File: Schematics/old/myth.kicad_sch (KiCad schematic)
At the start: 140 parts, among them J1 Conn_01x08_Male, J10 Conn_02x01, J2 Conn_01x08_Male, J3 Conn_01x08_Male, J4 Conn_01x08_Male, J5 Conn_01x08_Male, J6 Conn_01x08_Male, J7 Conn_01x08_Male, J8 Conn_01x04_Male, J9 Conn_01x04_Male, U1 74AHC02, U10 74HC595, U11 74HC165, U12 74AHC08, U13 74HC238, U14 74HC238, U15 74HC238, U16 4002, U17 74AHC273, U18 74LS32, U19 CD4532BE, U2 74AHC04, U20 74AHC138, U21 74AHC04, U22 74AHC138, U23 74HC238, U24 74HC238, U25 74LS32, U26 4078, U27 74AHC244, U28 74LS08, U29 74AHC138, U3 74HC74, U30 74AHC138, U31 4075, U32 74AHC04, U33 74HC00, U34 74HC163, U35 74AHC138, U36 74AHC138, U37 74HC238, U38 74AHC138, U39 74HC238, U4 74HC32, U40 74AHC02, U41 74AHC574, U42 74HC283, U43 74HC283, U44 74AHC574, U45 74HC193, U46 74HC193, U47 74HC157, U48 74HC157, U49 74HC32, U5 74AHC273, U50 74AHC244, U51 74HC157, U52 74HC157, U53 74HC157, U54 74HC157, U55 74HC02, U56 74HC74, U57 74HC193, U58 74HC193, U59 74HC04, U6 74LS08, U60 4078, U61 4078, U62 74AHC574, U63 74HC193, U64 74HC193, U65 74AHC273, U66 74AHC273, U67 74LS573, U68 74LS21, U69 74AHC244, U7 74AHC08, U70 74AHC04, U71 74AHC04, U72 74LS32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

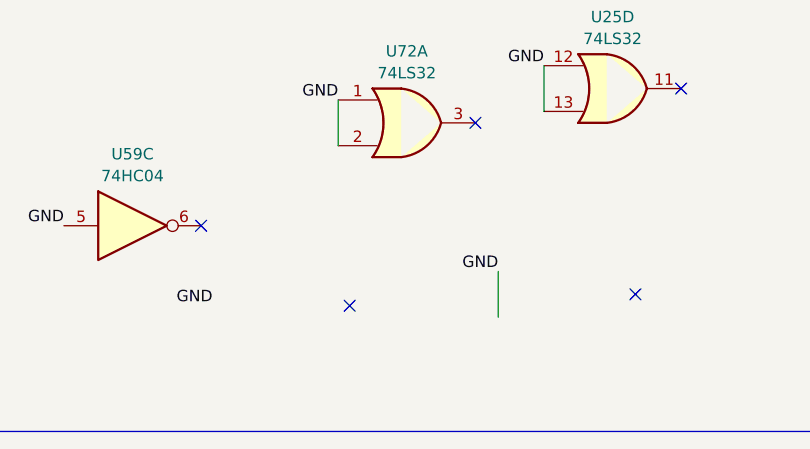
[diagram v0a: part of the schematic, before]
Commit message: Change d to g
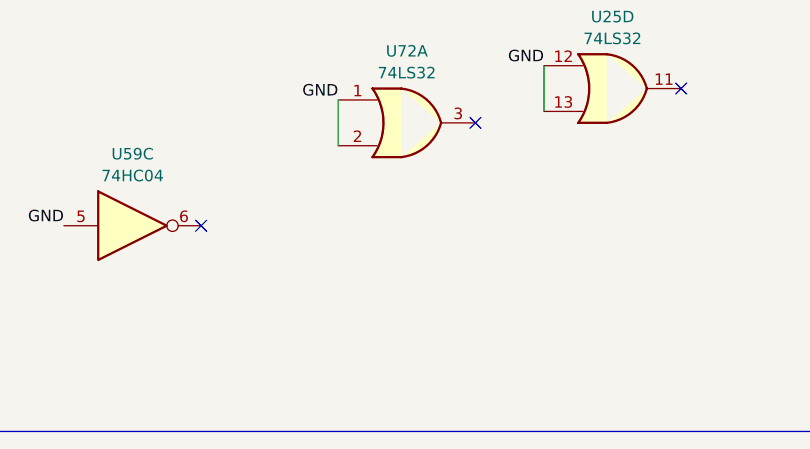
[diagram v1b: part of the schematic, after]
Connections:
- no-connect marks 69 -> 67
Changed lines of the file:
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@@
 	)
 	(no_connect
-		(at 965.2 806.45)
-	)
-	(no_connect
 		(at 137.16 384.81)
 	)
 	(no_connect
-		(at 996.95 805.18)
-	)
-	(no_connect
 		(at 128.27 95.25)
 	)
@@
 	(wire
 		(pts
-			(xy 981.71 802.64) (xy 981.71 807.72)
-		)
-		(stroke
-			(width 0)
-			(type default)
-		)
-	)
-	(wire
-		(pts
 			(xy 227.33 514.35) (xy 227.33 519.43)
 		)
@@
 		)
 	)
-	(label "GND"
-		(at 981.71 802.64 180)
-		(fields_autoplaced yes)
-		(effects
-			(font
-				(size 1.27 1.27)
-			)
-			(justify right bottom)
-		)
-	)
 	(label "+5V"
 		(at 71.12 107.95 180)
@@
 		(fields_autoplaced yes)
 		(effects
-			(font
-				(size 1.27 1.27)
-			)
-			(justify right bottom)
-		)
-	)
-	(label "GND"
-		(at 949.96 806.45 180)
-		(fields_autoplaced yes)
-		(effects

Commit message: Fix bugs in vtable.c
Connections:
- net GETD renamed GETG
- net xD renamed xG
- net ~{BOD} renamed ~{BOG}
- net ~{COD} renamed ~{COG}
- net ~{Dx} renamed ~{Gx}
- net ~{GETD} renamed ~{GETG}
- net ~{PUTD} renamed ~{PUTG}
- net ~{opc_DIRO} renamed ~{opc_GIRO}
- net ~{xD} renamed ~{xG}
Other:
- note added: "(Global) Page Index"
- note added: "G"
- note added: "G/I/R/O"
- note added: "Instruction byte: all0: OPC_SYS 00000 xxx See table @ SYS decoder else: OPC_FIX 00001 x xx b0-1 LSB, b2: Extended sign bit OPC_ALU 0001 xxxx See table @ ALU OPC_TRAP 001 xxxxx b0-4: DEST PAGE OPC_GIRO 01 xx x xxx b0-2 OFFS, b3:GET/PUT, B4-5:REG(GIRO) OPC_PAIR 1 xxx xxxx b0-3 DST, b4-6 SRC"
- note removed: "(DATA) Page Index"
- note removed: "D"
- note removed: "D/I/R/O"
- note removed: "Instruction byte: all0: OPC_SYS 00000 xxx See table @ SYS decoder else: OPC_FIX 00001 x xx b0-1 LSB, b2: Extended sign bit OPC_ALU 0001 xxxx See table @ ALU OPC_TRAP 001 xxxxx b0-4: DEST PAGE OPC_DIRO 01 xx x xxx b0-2 OFFS, b3:GET/PUT, B4-5:REG(DIRO) OPC_PAIR 1 xxx xxxx b0-3 DST, b4-6 SRC"
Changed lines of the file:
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@@
 		)
 	)
-	(text "(DATA)\nPage Index"
+	(text "(Global)\nPage Index"
 		(exclude_from_sim no)
 		(at 886.46 523.24 0)
@@
 		)
 	)
-	(text "D"
+	(text "G"
 		(exclude_from_sim no)
 		(at 871.22 525.78 0)
@@
 		)
 	)
-	(text "                Instruction byte:\nall0: OPC_SYS       00000   xxx    See table @ SYS decoder\nelse: OPC_FIX       00001  x xx    b0-1 LSB, b2: Extended sign bit\n      OPC_ALU       0001   xxxx    See table @ ALU\n      OPC_TRAP      001   xxxxx    b0-4: DEST PAGE\n      OPC_DIRO      01 xx x xxx    b0-2 OFFS, b3:GET/PUT, B4-5:REG(DIRO)\n      OPC_PAIR      1  xxx xxxx    b0-3 DST, b4-6 SRC"
+	(text "                Instruction byte:\nall0: OPC_SYS       00000   xxx    See table @ SYS decoder\nelse: OPC_FIX       00001  x xx    b0-1 LSB, b2: Extended sign bit\n      OPC_ALU       0001   xxxx    See table @ ALU\n      OPC_TRAP      001   xxxxx    b0-4: DEST PAGE\n      OPC_GIRO      01 xx x xxx    b0-2 OFFS, b3:GET/PUT, B4-5:REG(GIRO)\n      OPC_PAIR      1  xxx xxxx    b0-3 DST, b4-6 SRC"
 		(exclude_from_sim no)
 		(at 146.05 571.5 0)
@@
 		)
 	)
-	(text "D/I/R/O"
+	(text "G/I/R/O"
 		(exclude_from_sim no)
 		(at 321.31 471.17 0)
@@
 		)
 	)
-	(label "~{GETD}"
+	(label "~{GETG}"
 		(at 746.76 204.47 180)
 		(fields_autoplaced yes)
@@
 		)
 	)
-	(label "~{COD}"
+	(label "~{COG}"
 		(at 808.99 506.73 180)
 		(fields_autoplaced yes)
@@
 		)
 	)
-	(label "~{GETD}"
+	(label "~{GETG}"
 		(at 353.06 469.9 0)
 		(fields_autoplaced yes)
@@
 		)
 	)
-	(label "~{opc_DIRO}"
+	(label "~{opc_GIRO}"
 		(at 254 504.19 0)
 		(fields_autoplaced yes)
@@
 		)
 	)
-	(label "~{BOD}"
+	(label "~{BOG}"
 		(at 834.39 453.39 0)
 		(fields_autoplaced yes)
@@
 		)
 	)
-	(label "GETD"
+	(label "GETG"
 		(at 762 204.47 0)
 		(fields_autoplaced yes)
@@
 		)
 	)
-	(label "~{Dx}"
+	(label "~{Gx}"
 		(at 361.95 381 0)
 		(fields_autoplaced yes)
@@
 		)
 	)
-	(label "~{opc_DIRO}"
+	(label "~{opc_GIRO}"
 		(at 304.8 480.06 180)
 		(fields_autoplaced yes)
@@
 		)
 	)
-	(label "~{Dx}"
+	(label "~{Gx}"
 		(at 871.22 478.79 0)
 		(fields_autoplaced yes)
@@
 		)
 	)
-	(label "~{PUTD}"
+	(label "~{PUTG}"
 		(at 886.46 481.33 0)
 		(fields_autoplaced yes)
@@
 		)
 	)
-	(label "~{COD}"
+	(label "~{COG}"
 		(at 834.39 448.31 0)
 		(fields_autoplaced yes)
@@
 		)
 	)
-	(label "~{xD}"
+	(label "~{xG}"
 		(at 706.12 218.44 180)
 		(fields_autoplaced yes)
@@
 		)
 	)
-	(label "xD"
+	(label "xG"
 		(at 721.36 218.44 0)
 		(fields_autoplaced yes)
@@
 		)
 	)
-	(label "xD"
+	(label "xG"
 		(at 787.4 499.11 180)
 		(fields_autoplaced yes)
@@
 		)
 	)
-	(label "~{xD}"
+	(label "~{xG}"
 		(at 364.49 271.78 0)
 		(fields_autoplaced yes)
@@
 		)
 	)
-	(label "~{PUTD}"
+	(label "~{PUTG}"
 		(at 353.06 480.06 0)
 		(fields_autoplaced yes)
@@
 		)
 	)
-	(label "GETD"
+	(label "GETG"
 		(at 787.4 504.19 180)
 		(fields_autoplaced yes)
@@
 		)
 	)
-	(label "~{BOD}"
+	(label "~{BOG}"
 		(at 808.99 509.27 180)
 		(fields_autoplaced yes)

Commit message: Change E register semantics
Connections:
- net GND: no longer U59.5
- net ~{SL1_PAROE}: now also U59.6; no longer U29.14 (O1)
- net ~{SL10} renamed SL10
- net ~{SL11} renamed SL11
- net ~{SL12} renamed SL12
- net ~{SL13} renamed SL13
- net ~{SL14} renamed SL14
- net ~{SL15} renamed SL15
- net ~{SL2} renamed SL2
- net ~{SL3} renamed SL3
- net ~{SL4} renamed SL4
- net ~{SL5} renamed SL5
- net ~{SL6} renamed SL6
- net ~{SL7} renamed SL7
- net ~{SL8} renamed SL8
- net ~{SL9} renamed SL9
- new net SL1_PAROE: U29.14 (O1), U59.5
- no-connect marks 67 -> 66
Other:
- note added: "SL0_NULL device"
- note removed: "~{SL0_NULL} device"
- moved on the sheet: U21A, U21B, U21C, U21E, U32B, U32C, U32D, U32E, U32F, U59B, U59C, U59E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

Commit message: Change CO do D
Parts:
- removed U29, U30: 74AHC138, Package_DIP:DIP-16_W7.62mm_Socket_LongPads, symbol 74xx:74LS138
- added U29, U30: 74HC238, Package_DIP:DIP-16_W7.62mm_Socket_LongPads, symbol 74xx_IEEE:74HC238
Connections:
- net +5V: now also U29.16 (VCC), U29.6 (G1), U30.16 (VCC)
- net EL0: now also U29.1 (A0), U30.1 (A0)
- net EL1: now also U29.2 (A1), U30.2 (A1)
- net EL2: now also U29.3 (A2), U30.3 (A2)
- net EL3: now also U30.6 (G1)
- net GND: now also U29.5 (~{G2B}), U29.8 (GND), U30.4 (~{G2A}), U30.5 (~{G2B}), U30.8 (GND)
- net SL10: now also U30.13 (Y2)
- net SL11: now also U30.12 (Y3)
- net SL12: now also U30.11 (Y4)
- net SL13: now also U30.10 (Y5)
- net SL14: now also U30.9 (Y6)
- net SL15: now also U30.7 (Y7)
- net SL1_PAROE: now also U29.14 (Y1)
- net SL2: now also U29.13 (Y2)
- net SL3: now also U29.12 (Y3)
- net SL4: now also U29.11 (Y4)
- net SL5: now also U29.10 (Y5)
- net SL6: now also U29.9 (Y6)
- net SL7: now also U29.7 (Y7)
- net SL8: now also U30.15 (Y0)
- net SL9: now also U30.14 (Y1)
- new net EHL: U29.4 (~{G2A})
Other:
- note added: "(DUPE) Register"
- note added: "D"
- note added: "HIGH ORDER SELECTOR"
- note added: "LOW ORDER SELECTOR"
- note removed: "ACTIVE HIGH ENABLE"
- note removed: "ACTIVE LOW ENABLE"
- note removed: "Co"
- note removed: "LOX: SMEMA0LE"
- note removed: "LOX: SMEMA1LE"
- note removed: "LOX: SMEMA2LE"
- note removed: "LOX: SMEMOE"
- note removed: "LOX: SMEMWE"
- note removed: "SH0_NULL device"
- note removed: "SL0_NULL device"
- moved on the sheet: U23, U24, U2B, U2D

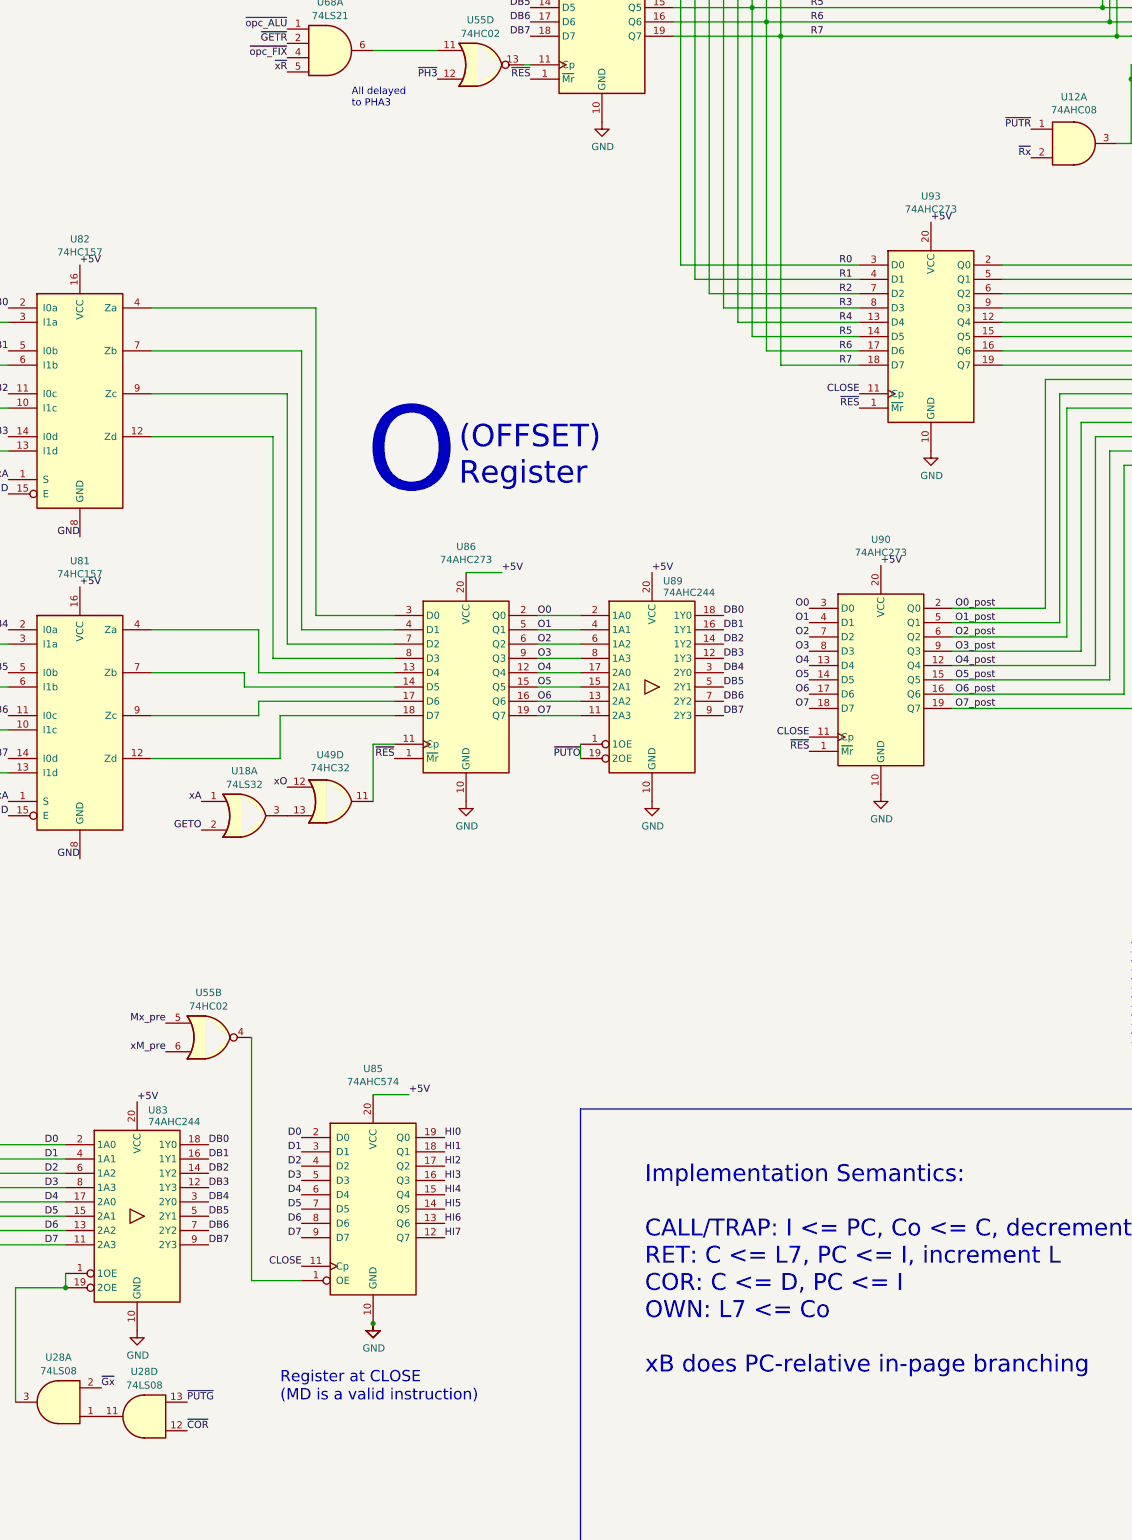
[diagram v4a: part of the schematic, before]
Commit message: Change COR to use R
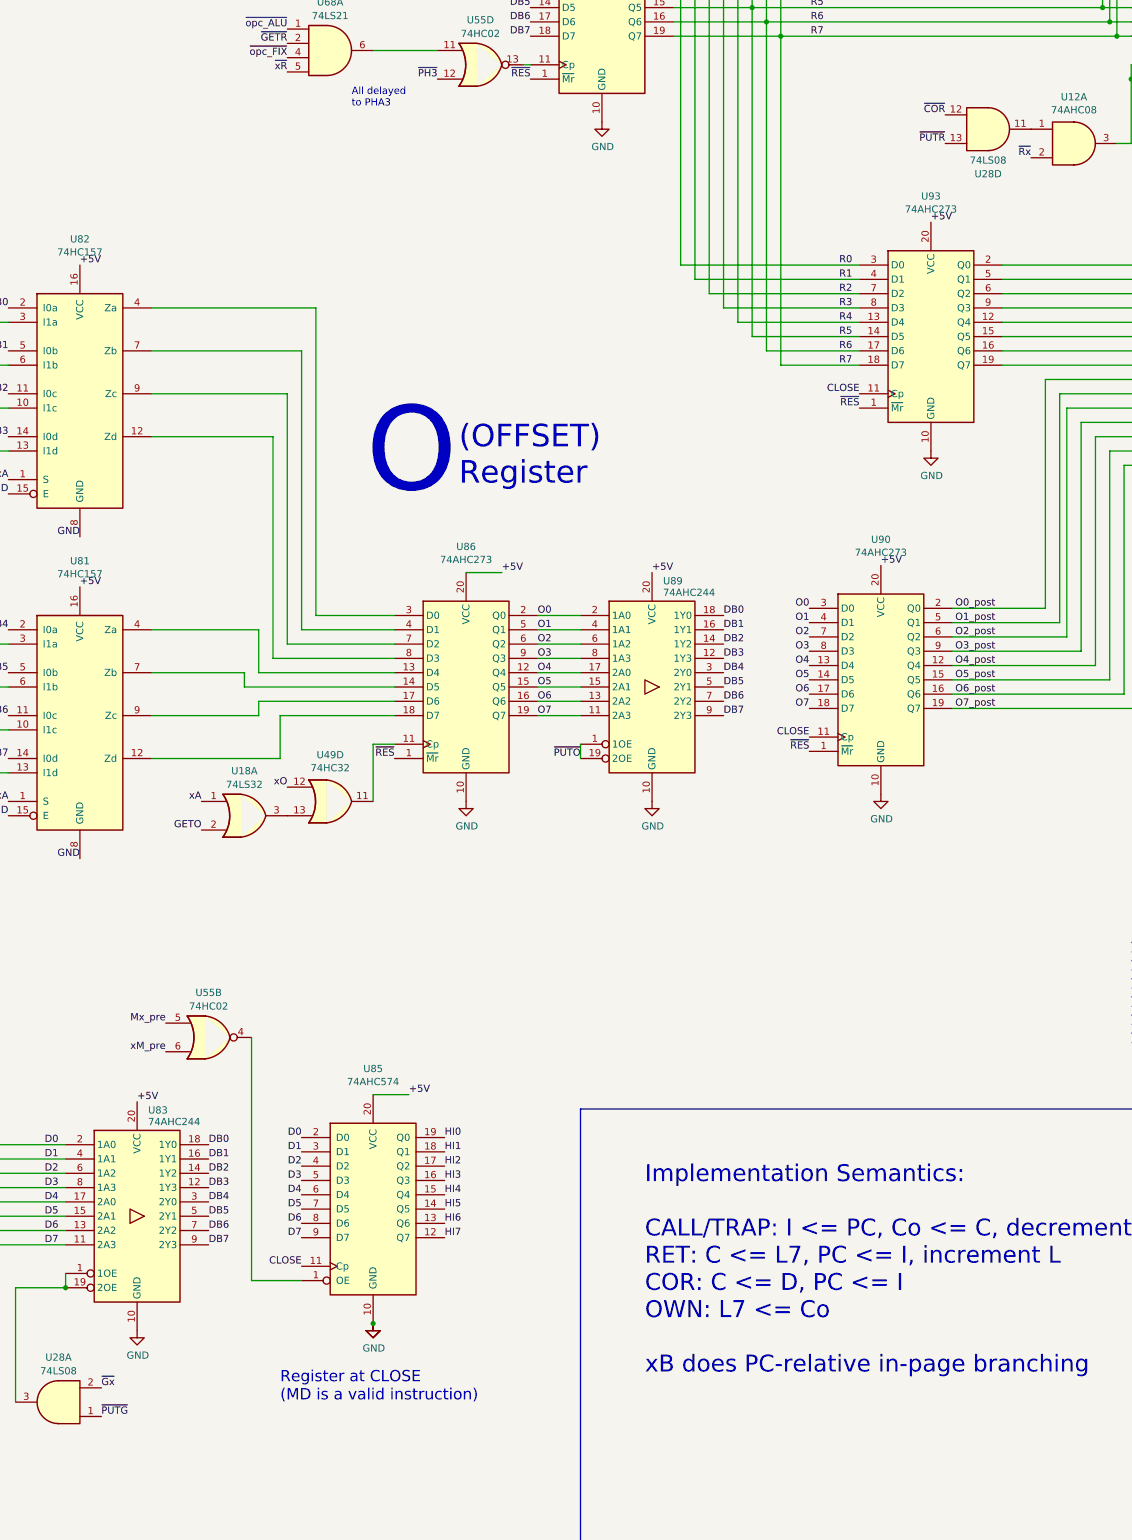
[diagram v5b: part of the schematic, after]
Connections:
- net ~{PUTG}: now also U28.1; no longer U28.13
- net ~{PUTR}: now also U28.13; no longer U12.1
- net at U28.11: now also U12.1; no longer U28.1
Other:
- moved on the sheet: U28D
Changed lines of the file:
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@@
 	(title_block
 		(title "Sonne-8 Micro-Controller")
-		(date "2024-10-12")
+		(date "2024-10-14")
 		(rev "Myth")
 		(company "Contact: mim@ok-schalter.de")
@@
 	)
 	(label "~{COR}"
-		(at 886.46 486.41 0)
+		(at 1021.08 252.73 180)
 		(fields_autoplaced yes)
 		(effects
@@
 				(size 1.27 1.27)
 			)
-			(justify left bottom)
+			(justify right bottom)
 		)
 	)
@@
 	)
 	(label "~{PUTG}"
-		(at 886.46 481.33 0)
+		(at 871.22 483.87 0)
 		(fields_autoplaced yes)
 		(effects
@@
 	)
 	(label "~{PUTR}"
-		(at 1036.32 255.27 180)
+		(at 1021.08 257.81 180)
 		(fields_autoplaced yes)
 		(effects
@@
 	(symbol
 		(lib_id "74xx:74LS08")
-		(at 878.84 483.87 180)
+		(at 1028.7 255.27 0)
 		(unit 4)
 		(exclude_from_sim no)
@@
 		(fields_autoplaced yes)
 		(property "Reference" "U28"
-			(at 878.8483 475.9155 0)
+			(at 1028.6917 263.2245 0)
 			(effects
 				(font
@@
 		)
 		(property "Value" "74LS08"
-			(at 878.8483 478.3398 0)
+			(at 1028.6917 260.8002 0)
 			(effects
 				(font
@@
 		)
 		(property "Footprint" "Package_DIP:DIP-14_W7.62mm_Socket_LongPads"
-			(at 878.84 483.87 0)
+			(at 1028.7 255.27 0)
 			(effects
 				(font
@@
 		)
 		(property "Datasheet" "http://www.ti.com/lit/gpn/sn74LS08"
-			(at 878.84 483.87 0)
+			(at 1028.7 255.27 0)
 			(effects
 				(font
@@
 		)
 		(property "Description" "Quad And2"
-			(at 878.84 483.87 0)
+			(at 1028.7 255.27 0)
 			(effects
 				(font
